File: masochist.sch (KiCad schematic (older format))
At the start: 62 parts, among them Y1 Crystal

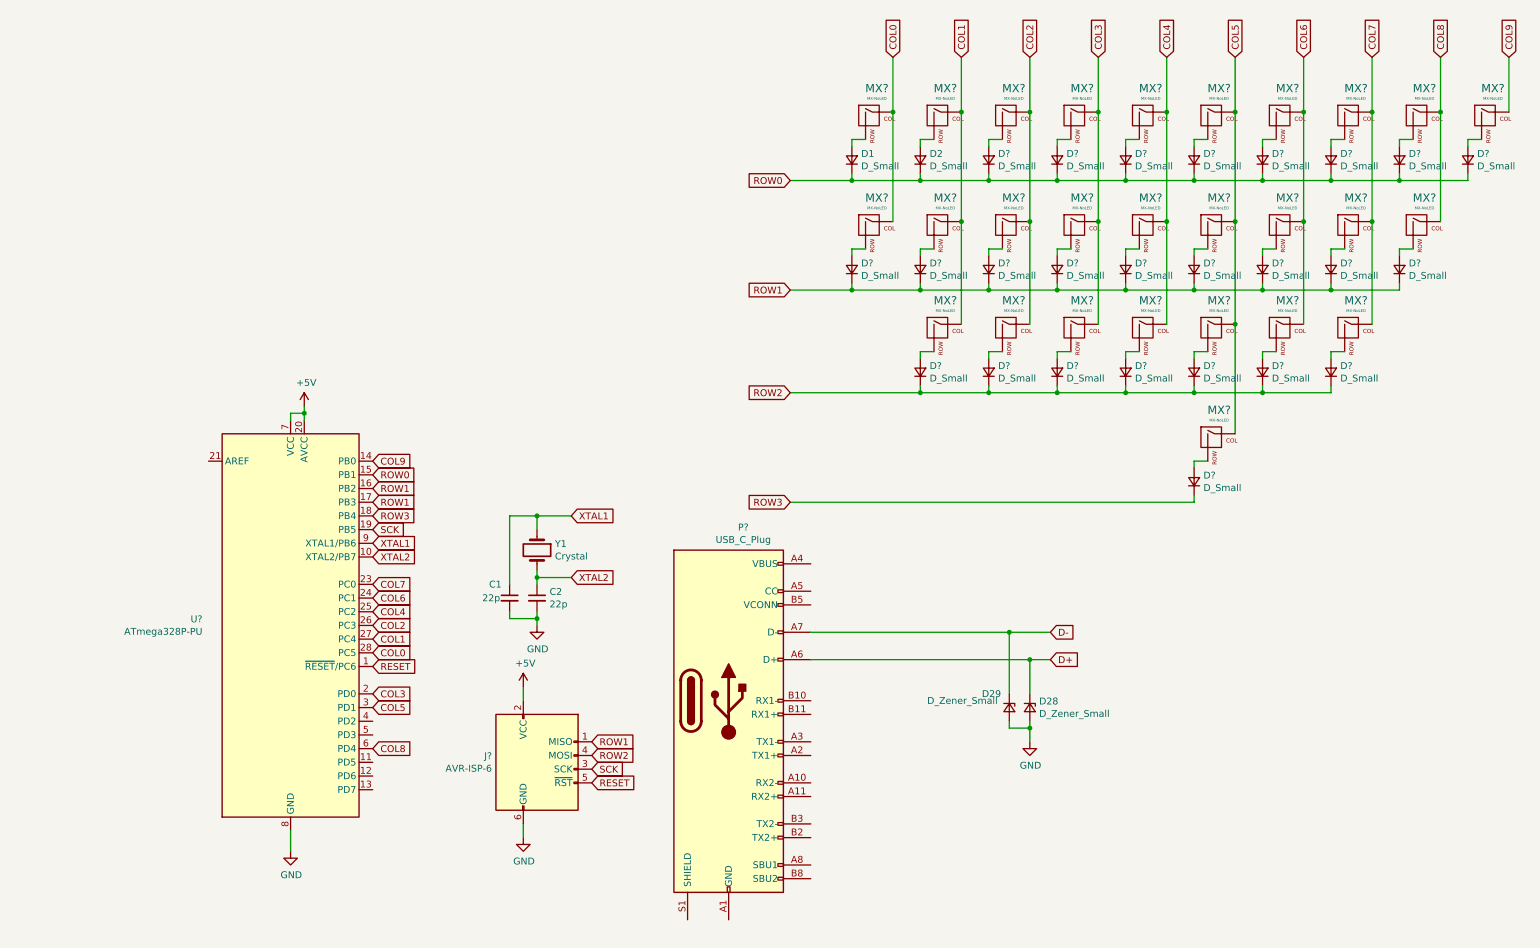
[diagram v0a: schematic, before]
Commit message: switched to USB-C 2.0 receptacle and wired it up
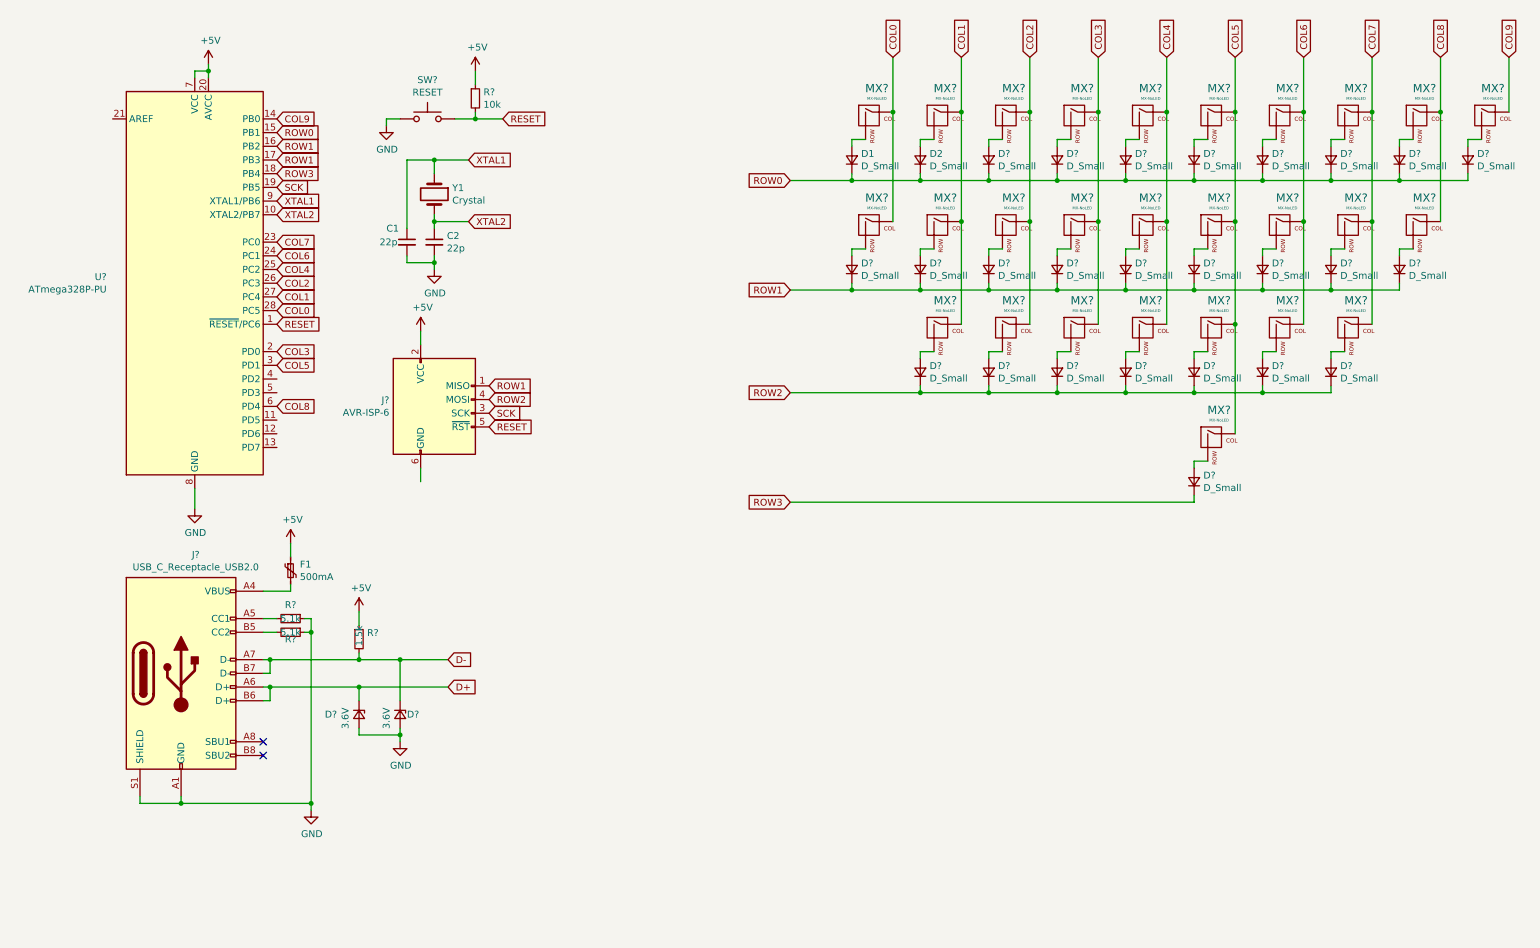
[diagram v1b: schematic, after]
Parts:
- removed D28, D29: D_Zener_Small, symbol Device:D_Zener_Small
- removed P?: USB_C_Plug, symbol Connector:USB_C_Plug
- added D? (x2): 3.6V, symbol Device:D_Zener_Small
- added F1: 500mA, symbol Device:Polyfuse_Small
- added J?: USB_C_Receptacle_USB2.0, symbol Connector:USB_C_Receptacle_USB2.0
- added R?: 10k, symbol Device:R_Small
- added R? (x2): 5.1k, symbol Device:R_Small
- added R?: 1.5k, symbol Device:R_Small
- added SW?: RESET, symbol Switch:SW_Push
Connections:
- net +5V: now also F1.1, R?.1, R?.1
- net D+: now also D?.1 (K), J?.A6 (D+), J?.B6 (D+)
- net D-: now also D?.1 (K), J?.A7 (D-), J?.B7 (D-), R?.2
- net GND: now also D?.2 (A), D?.2 (A), J?.A1 (GND), J?.A12 (GND), J?.B1 (GND), J?.B12 (GND), J?.S1 (SHIELD), R?.1, R?.1, SW?.1; no longer J?.6 (GND)
- net RESET: now also R?.2, SW?.2
- new net: F1.2, J?.A4 (VBUS), J?.A9 (VBUS), J?.B4 (VBUS), J?.B9 (VBUS)
- new net: J?.A5 (CC1), R?.2
- new net: J?.B5 (CC2), R?.2
- no-connect marks 0 -> 2
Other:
- moved on the sheet: C1, C2, J?, U?, Y1

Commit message: finished schematic??
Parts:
- added C3: 4.7u, symbol Device:CP1_Small
- added C4, C5: 0.1u, symbol Device:C_Small
- added LED1: POWER, symbol Device:LED_Small
- added R? (x2): 75, symbol Device:R_Small
- added R?: 1.5k, symbol Device:R_Small
- added SW?: SW_Push, symbol Switch:SW_Push
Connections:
- net +5V: now also C3.1, C4.1, C5.1, LED1.2 (A)
- net D+: now also R?.1; no longer D?.1 (K), J?.A6 (D+), J?.B6 (D+)
- net D-: now also R?.1; no longer D?.1 (K), J?.A7 (D-), J?.B7 (D-), R?.2
- net GND: now also J?.6 (GND), C3.2, C4.2, C5.2, R?.2, SW?.1
- new net: D?.1 (K), J?.A6 (D+), J?.B6 (D+), R?.2
- new net: D?.1 (K), J?.A7 (D-), J?.B7 (D-), R?.2, R?.2
- new net: LED1.1 (K), R?.1
- new net BOOT: SW?.2
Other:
- moved on the sheet: D?, F1, J?, R?
